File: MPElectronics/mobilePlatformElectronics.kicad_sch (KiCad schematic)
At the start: 90 parts, among them J1 UART, J2 UART, J3 Magnetic Encoder, J4 Magnetic Encoder, M1 Motor_DC, M2 Motor_DC, M3 Motor_DC, M4 Motor_DC, M5 SG90 9g Micro Servo, M6 RDS51150, M7 RDS51150, M8 SY35ST28-0504A_Stepper_Motor_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, Q1 LTR3208E, SW1 Reset, SW2 Reset, SW3 Reset, SW4 SW_SPDT, SW5 SW_SPDT, SW6 SW_SPDT_LIMIT, SW7 SW_SPDT_LIMIT, U1 PIC32MX170F256B, U10 TLE5206-2S, U12 IR Distance, U13 IR Distance, U14 L293NE/SN754410NE, U2 TLE5206-2S, U3 PIC32MX170F256B, U4 IR Line Sensor, U5 IR Line Sensor, U6 IR Line Sensor, U7 MCP6294, U8 LM339AN, U9 IR Line Sensor

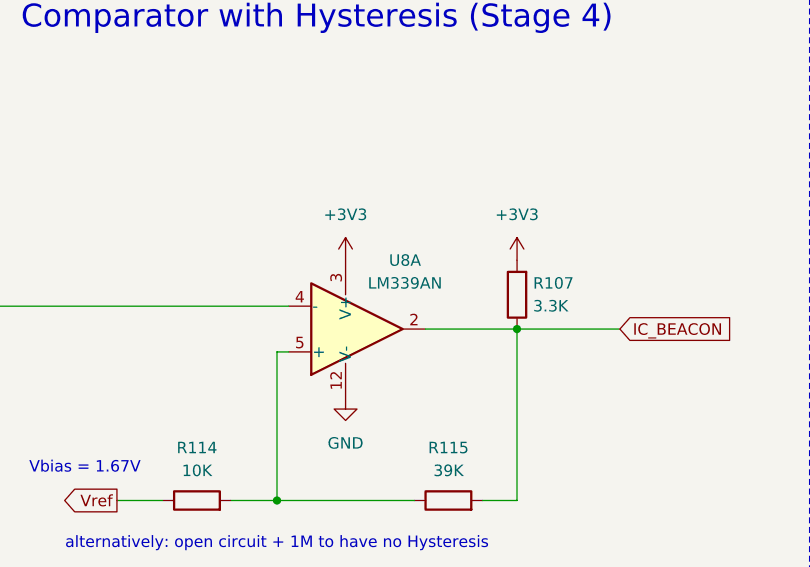
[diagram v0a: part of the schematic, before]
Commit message: update comparator
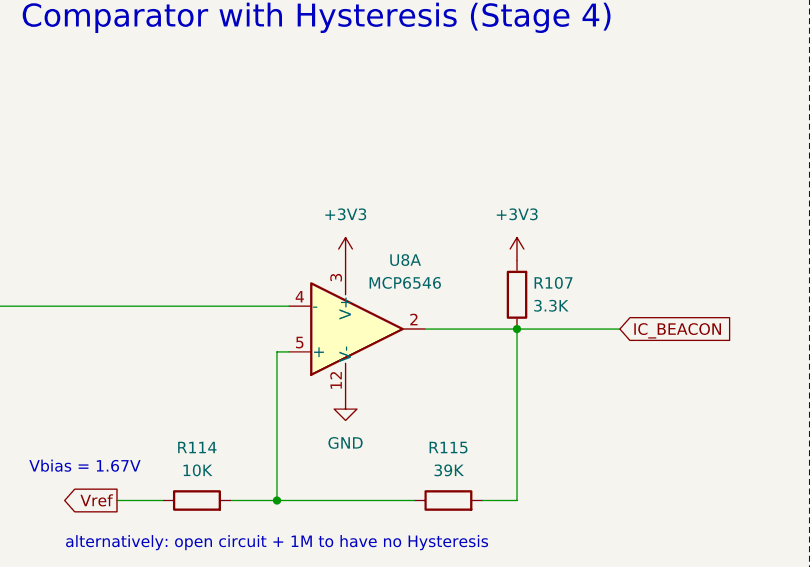
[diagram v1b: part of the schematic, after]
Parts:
- U8: value LM339AN -> MCP6546
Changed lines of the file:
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@@
 			)
 		)
-		(property "Value" "LM339AN"
+		(property "Value" "MCP6546"
 			(at 831.342 123.9519 0)
 			(effects
@@
 			)
 		)
-		(property "Value" "LM339AN"
+		(property "Value" "MCP6546"
 			(at 839.216 117.602 0)
 			(effects

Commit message: tune and update schematic
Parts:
- added C23: 10uF, symbol ME218_BaseLib:Cap
- R107: value 3.3K -> 10K
- R7: value 2K2 -> 200K
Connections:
- net GND: now also C23.2
- net at R8.1, R9.2, U7.5 (+): now also C23.1
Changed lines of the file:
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@@
 	(text "Vbias = 1.67V"
 		(exclude_from_sim no)
-		(at 901.954 114.808 0)
+		(at 899.414 112.776 0)
 		(effects
 			(font
@@
 	(wire
 		(pts
+			(xy 899.668 114.554) (xy 910.336 114.554)
+		)
+		(stroke
+			(width 0)
+			(type default)
+		)
+	)
+	(wire
+		(pts
 			(xy 765.048 295.148) (xy 765.048 296.418)
 		)
@@
 	(wire
 		(pts
+			(xy 899.668 114.554) (xy 899.668 115.824)
+		)
+		(stroke
+			(width 0)
+			(type default)
+		)
+	)
+	(wire
+		(pts
 			(xy 330.2 309.372) (xy 313.69 309.372)
 		)
@@
 	)
 	(symbol
+		(lib_id "power:GND")
+		(at 899.668 123.444 0)
+		(unit 1)
+		(exclude_from_sim no)
+		(in_bom yes)
+		(on_board yes)
+		(dnp no)
+		(fields_autoplaced yes)
+		(property "Reference" "#PWR019"
+			(at 899.668 129.794 0)
+			(effects
+				(font
+					(size 1.27 1.27)
+				)
+				(hide yes)
+			)
+		)
+		(property "Value" "GND"
+			(at 899.668 128.524 0)
+			(effects
+				(font
+					(size 1.27 1.27)
+				)
+			)
+		)
+		(property "Footprint" ""
+			(at 899.668 123.444 0)
+			(effects
+				(font
+					(size 1.27 1.27)
+				)
+				(hide yes)
+			)
+		)
+		(property "Datasheet" ""
+			(at 899.668 123.444 0)
+			(effects
+				(font
+					(size 1.27 1.27)
+				)
+				(hide yes)
+			)
+		)
+		(property "Description" "Power symbol creates a global label with name \"GND\" , ground"
+			(at 899.668 123.444 0)
+			(effects
+				(font
+					(size 1.27 1.27)
+				)
+				(hide yes)
+			)
+		)
+		(pin "1"
+		)
+		(instances
+			(project "mobilePlatformElectronics"
+				(path "/bd24c4db-4e36-4117-bd4f-5228ef241da9"
+					(reference "#PWR019")
+					(unit 1)
+				)
+			)
+		)
+	)
+	(symbol
 		(lib_id "ME218_BaseLib:Photo_NPN")
 		(at 555.498 113.792 0)
@@
 			)
 		)
-		(property "Value" "2K2"
+		(property "Value" "200K"
 			(at 624.332 104.14 90)
 			(effects
@@
 			)
 		)
-		(property "Value" "3.3K"
+		(property "Value" "10K"
 			(at 853.44 120.1419 0)
 			(effects
@@
 					(unit 1)
 				)
+			)
+		)
+	)
+	(symbol
+		(lib_id "ME218_BaseLib:Cap")
+		(at 899.668 119.634 0)
+		(unit 1)
+		(exclude_from_sim no)
+		(in_bom yes)
+		(on_board yes)
+		(dnp no)
+		(property "Reference" "C23"
+			(at 905.764 119.126 90)
+			(effects
+				(font
+					(size 1.27 1.27)
+				)
+			)
+		)
+		(property "Value" "10uF"
+			(at 903.478 119.38 90)
+			(effects
+				(font
+					(size 1.27 1.27)
+				)
+			)
+		)
+		(property "Footprint" ""
+			(at 900.6332 123.444 0)
+			(effects
+				(font
+					(size 1.27 1.27)
+				)
+				(hide yes)
+			)
+		)
+		(property "Datasheet" ""
+			(at 899.668 119.634 0)
+			(effects
+				(font
+					(size 1.27 1.27)
+				)
+				(hide yes)
+			)
+		)
+		(property "Description" ""
+			(at 899.668 119.634 0)
+			(effects
+				(font
+					(size 1.27 1.27)
+				)
+				(hide yes)
+			)
+		)
+		(pin "2"
+		)
+		(pin "1"
+		)
+		(instances
+			(project "mobilePlatformElectronics"
+				(path "/bd24c4db-4e36-4117-bd4f-5228ef241da9"
+					(reference "C23")
+					(unit 1)
+				)

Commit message: include enable pin for stepper (RB12)
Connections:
- net GND: no longer A1.9 (~{ENABLE})
- net M_FEEDER_EN: now reaches U3.23 (RB12)
- net M_FEEDER_EN: now also A1.9 (~{ENABLE})
- no-connect marks 12 -> 11
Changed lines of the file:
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@@
 	)
 	(junction
-		(at 463.296 308.356)
-		(diameter 0)
-		(color 0 0 0 0)
-	)
-	(junction
 		(at 303.53 344.932)
 		(diameter 0)
@@
 	)
 	(no_connect
-		(at 123.698 308.356)
-	)
-	(no_connect
 		(at 354.584 121.412)
 	)
@@
 	(wire
 		(pts
-			(xy 485.14 303.276) (xy 463.296 303.276)
-		)
-		(stroke
-			(width 0)
-			(type default)
-		)
-	)
-	(wire
-		(pts
 			(xy 355.854 93.98) (xy 355.854 103.886)
 		)
@@
 	(wire
 		(pts
+			(xy 482.6 303.276) (xy 485.14 303.276)
+		)
+		(stroke
+			(width 0)
+			(type default)
+		)
+	)
+	(wire
+		(pts
 			(xy 339.09 339.852) (xy 370.84 339.852)
 		)
@@
 	(wire
 		(pts
-			(xy 463.296 303.276) (xy 463.296 308.356)
-		)
-		(stroke
-			(width 0)
-			(type default)
-		)
-	)
-	(wire
-		(pts
 			(xy 687.578 132.588) (xy 687.578 135.89)
 		)
@@
 	(wire
 		(pts
+			(xy 133.604 308.356) (xy 123.698 308.356)
+		)
+		(stroke
+			(width 0)
+			(type default)
+		)
+	)
+	(wire
+		(pts
 			(xy 354.584 108.712) (xy 355.854 108.712)
 		)
@@
 		)
 	)
+	(global_label "M_FEEDER_EN"
+		(shape input)
+		(at 133.604 308.356 0)
+		(fields_autoplaced yes)
+		(effects
+			(font
+				(size 1.27 1.27)
+			)
+			(justify left)
+		)
+		(property "Intersheetrefs" "${INTERSHEET_REFS}"
+			(at 149.5309 308.356 0)
+			(effects
+				(font
+					(size 1.27 1.27)
+				)
+				(justify left)
+				(hide yes)
+			)
+		)
+	)
 	(global_label "Vref"
 		(shape output)
@@
 			(effects
 				(font
+					(size 1.27 1.27)
+				)
+				(justify right)
+				(hide yes)
+			)
+		)
+	)
+	(global_label "M_FEEDER_EN"
+		(shape output)
+		(at 482.6 303.276 180)
+		(fields_autoplaced yes)
+		(effects
+			(font
+				(size 1.27 1.27)
+			)
+			(justify right)
+		)
+		(property "Intersheetrefs" "${INTERSHEET_REFS}"
+			(at 466.6731 303.276 0)
+			(effects
+				(font

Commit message: schematic updates and annotation for perf board assembly
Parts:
- removed SW5: SW_SPDT, symbol Switch:SW_SPDT
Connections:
- net NP_STRIP: no longer U3.14 (PGED3/5VT/RB5)
- net DIN_STRATEGY: no longer names the net of U3.12 (RA4)
- no-connect marks 11 -> 19
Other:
- note added: "Limit switch off to the subsystem From the perf board, the green node and the ground pin go out to the limit switch with a molex"
